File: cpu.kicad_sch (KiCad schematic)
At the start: 37 parts, among them J11 Debug, J12 GPS_Snoop, J13 I2C_Snoop, J7 USB_C_Receptacle_16P, U4 STM32H503KBUx, Y1 32768Hz

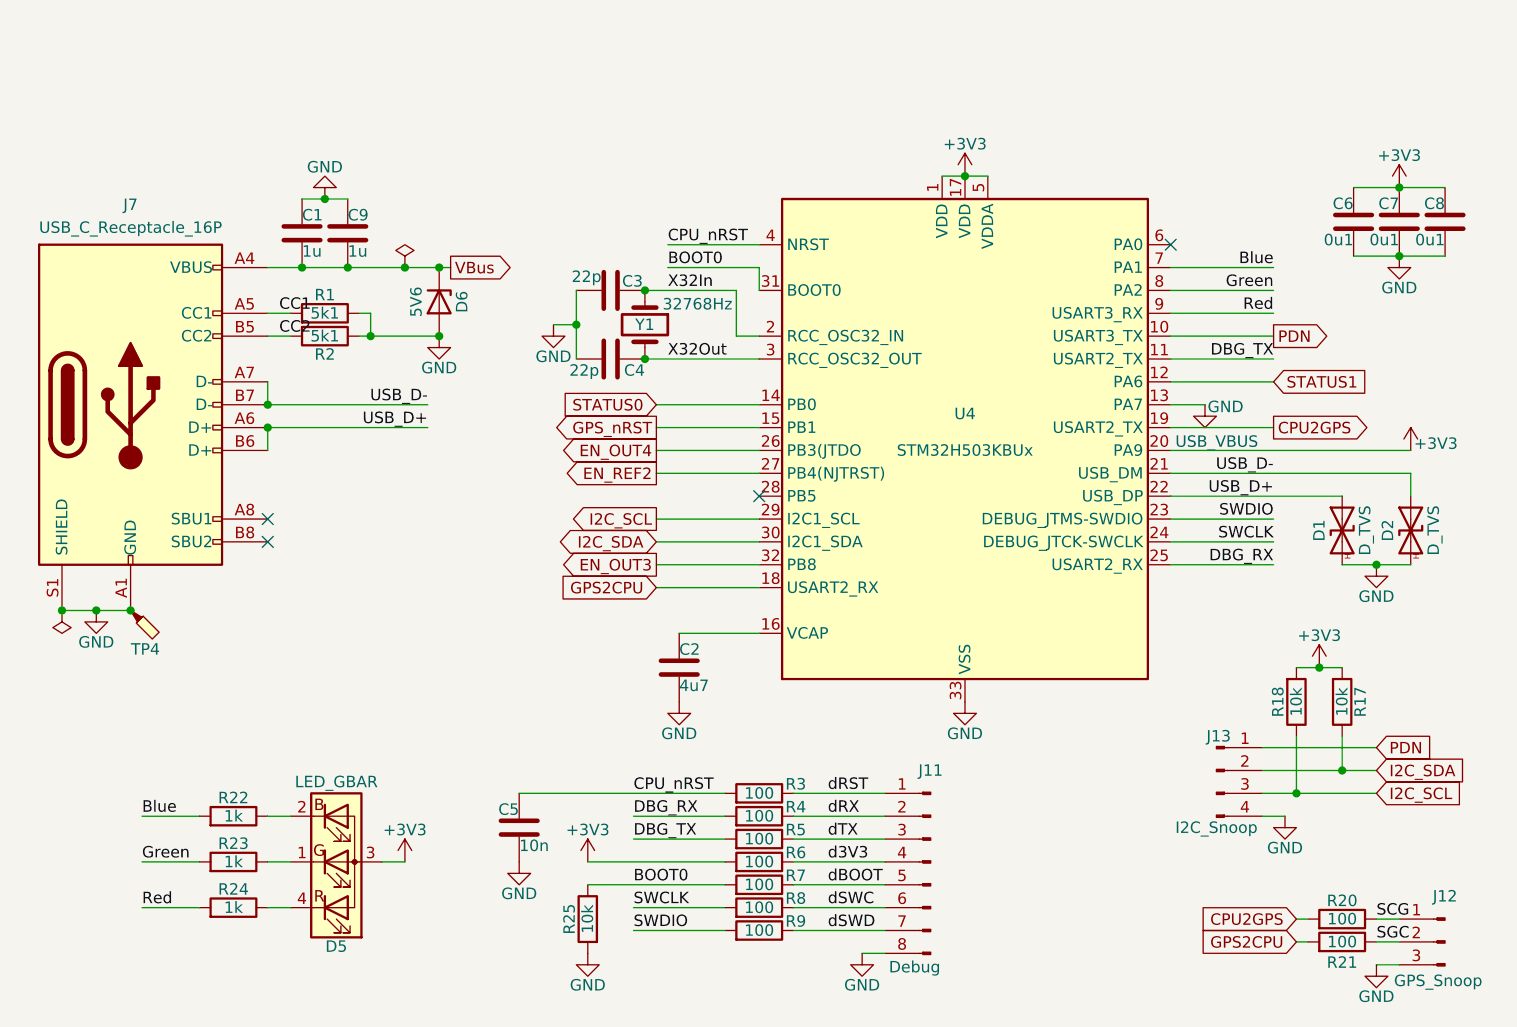
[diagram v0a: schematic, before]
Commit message: Squeeze in a connector to break out GPS.
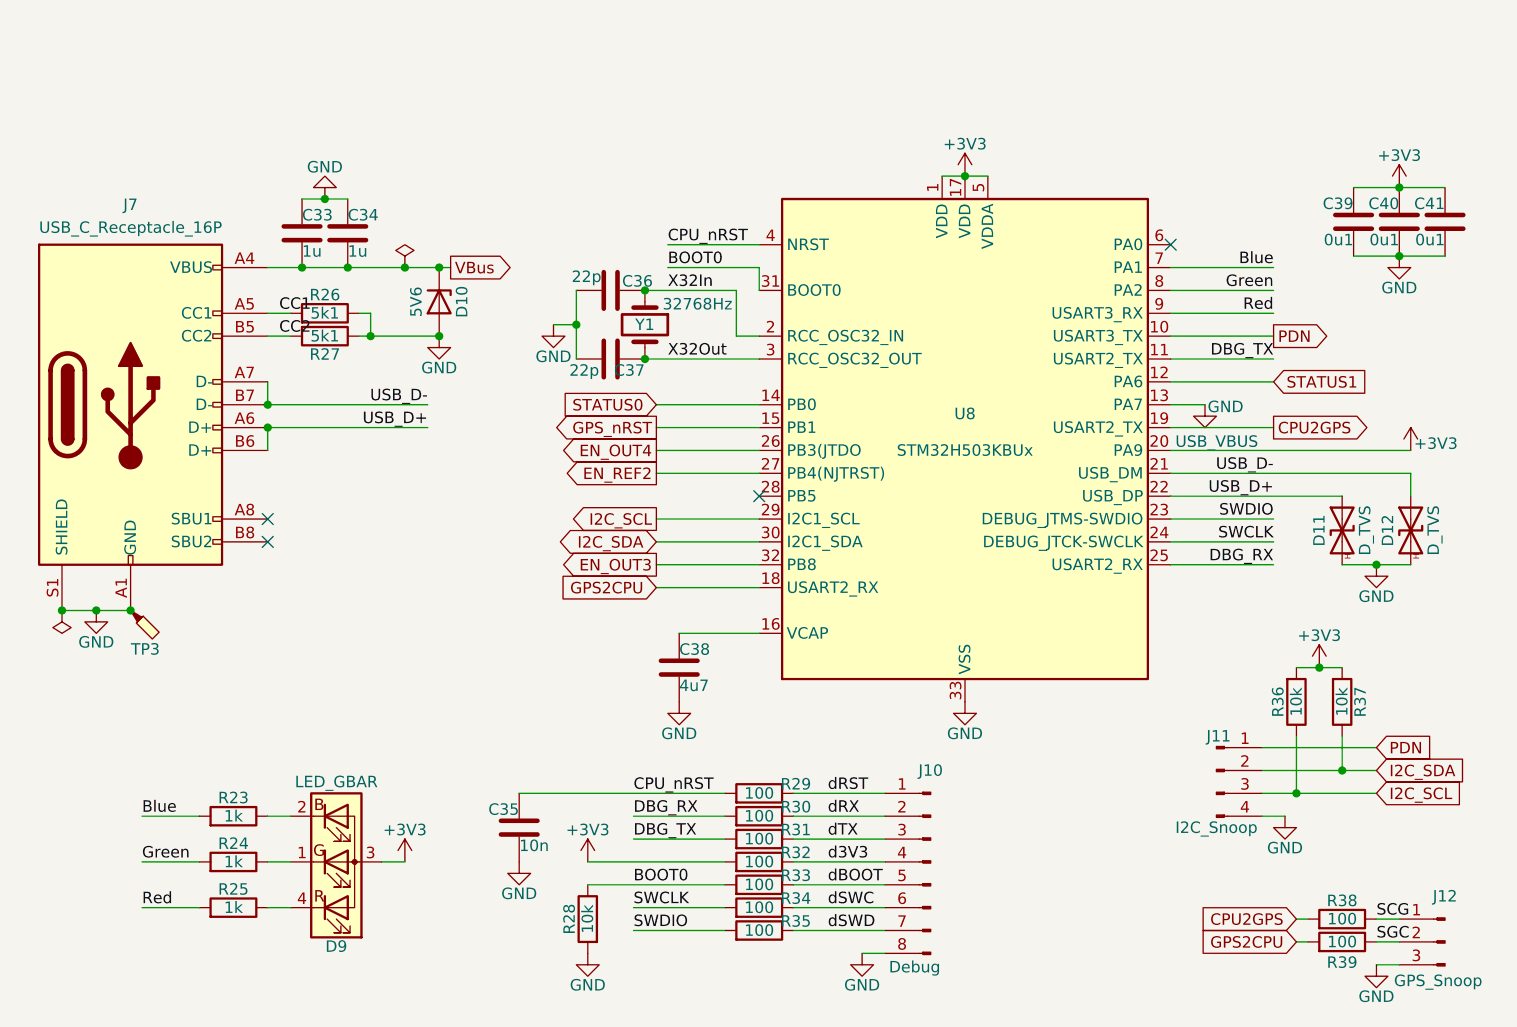
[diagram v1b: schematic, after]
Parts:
- renumbered C1 to C33, C9 to C34, C5 to C35, C3 to C36, C4 to C37, C2 to C38, C6 to C39, C7 to C40, C8 to C41, D6 to D10, D1 to D11, D2 to D12, D5 to D9, J11 to J10, J13 to J11, R22 to R23, R23 to R24, R24 to R25, R1 to R26, R2 to R27, R25 to R28, R3 to R29, R4 to R30, R5 to R31, R6 to R32, R7 to R33, R8 to R34, R9 to R35, R18 to R36, R17 to R37, R20 to R38, R21 to R39, TP4 to TP3, U4 to U8

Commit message: Silkscreen passes DRC.  Also we renumbered everything.
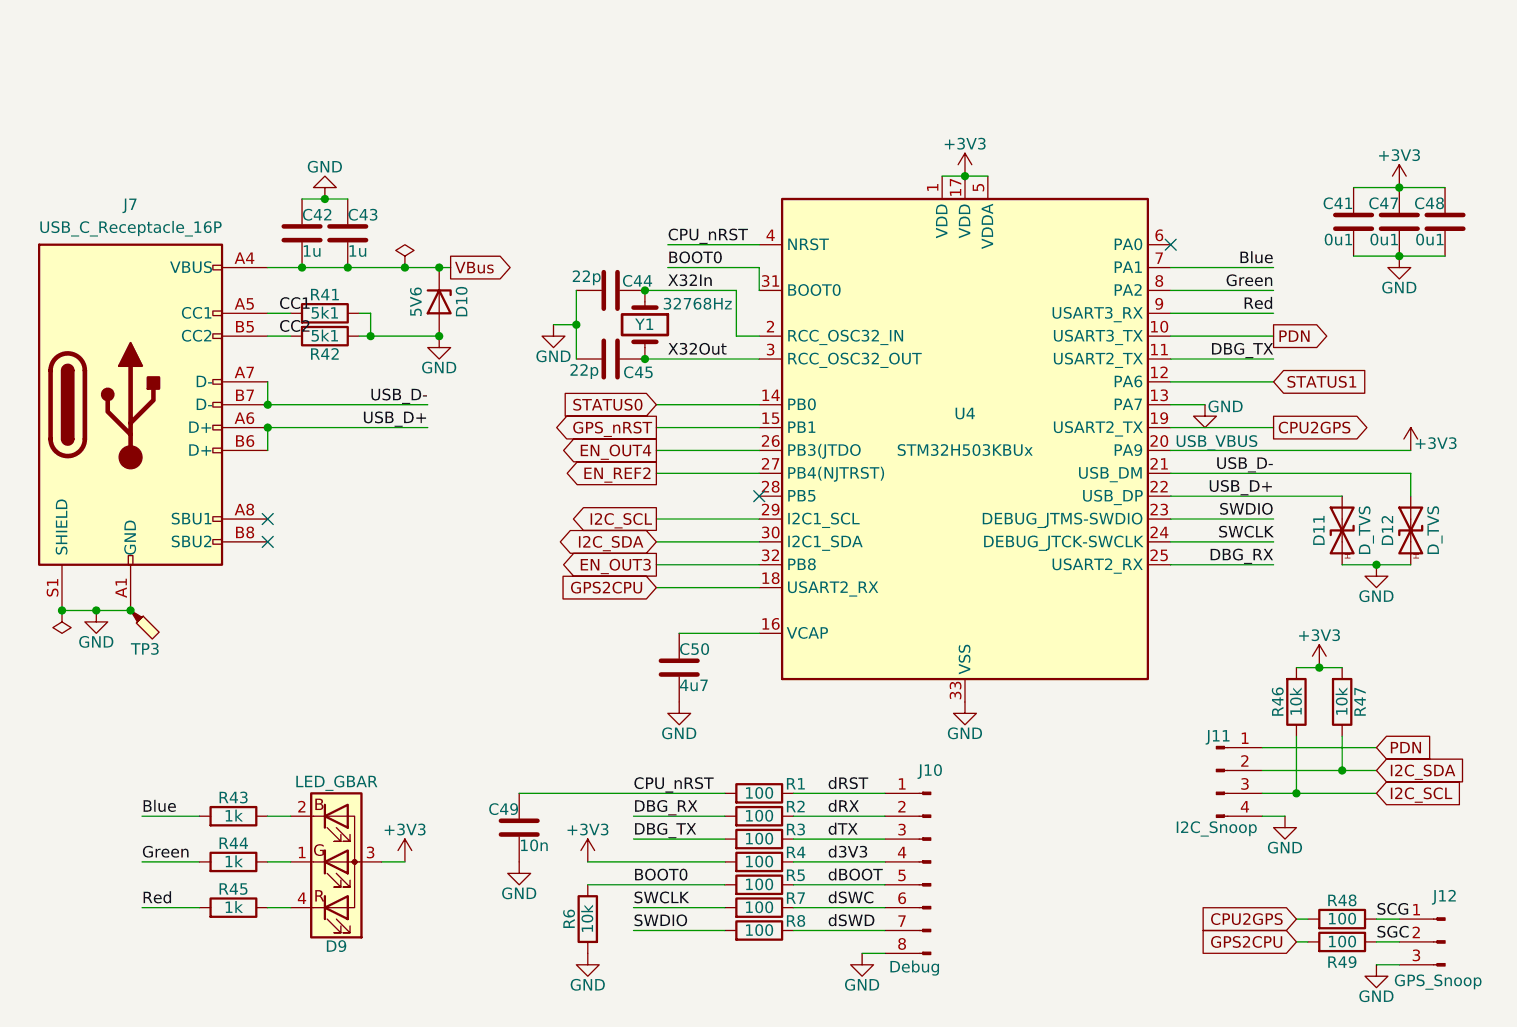
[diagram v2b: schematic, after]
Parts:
- renumbered C39 to C41, C33 to C42, C34 to C43, C36 to C44, C37 to C45, C40 to C47, C41 to C48, C35 to C49, C38 to C50, R29 to R1, R30 to R2, R31 to R3, R32 to R4, R26 to R41, R27 to R42, R23 to R43, R24 to R44, R25 to R45, R36 to R46, R37 to R47, R38 to R48, R39 to R49, R33 to R5, R28 to R6, R34 to R7, R35 to R8, U8 to U4

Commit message: Sorting out part number assignments.
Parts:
- C41, C47, C48: JLCPCB C307331 -> (none); LCSC (none) -> C307331
- C42, C43: JLCPCB C52923 -> (none); LCSC (none) -> C52923
- C44, C45: JLCPCB C1555 -> (none); LCSC (none) -> C1555
- C49: JLCPCB C15195 -> (none); LCSC (none) -> C15195
- C50: JLCPCB C23733 -> (none); LCSC (none) -> C23733
- D10: JLCPCB C19077435 -> (none); LCSC (none) -> C19077435
- R1, R2, R3, R4, R48, R49, R5, R7, R8: JLCPCB C25076 -> (none); LCSC (none) -> C25076
- R41, R42: JLCPCB C25905 -> (none); LCSC (none) -> C25905
- R43, R44, R45: JLCPCB C11702 -> (none); LCSC (none) -> C11702
- R46, R47, R6: JLCPCB C25744 -> (none); LCSC (none) -> C25744
- U4: JLCPCB C22385521 -> (none); LCSC (none) -> C22385521
- Y1: JLCPCB C32346 -> (none); LCSC (none) -> C32346

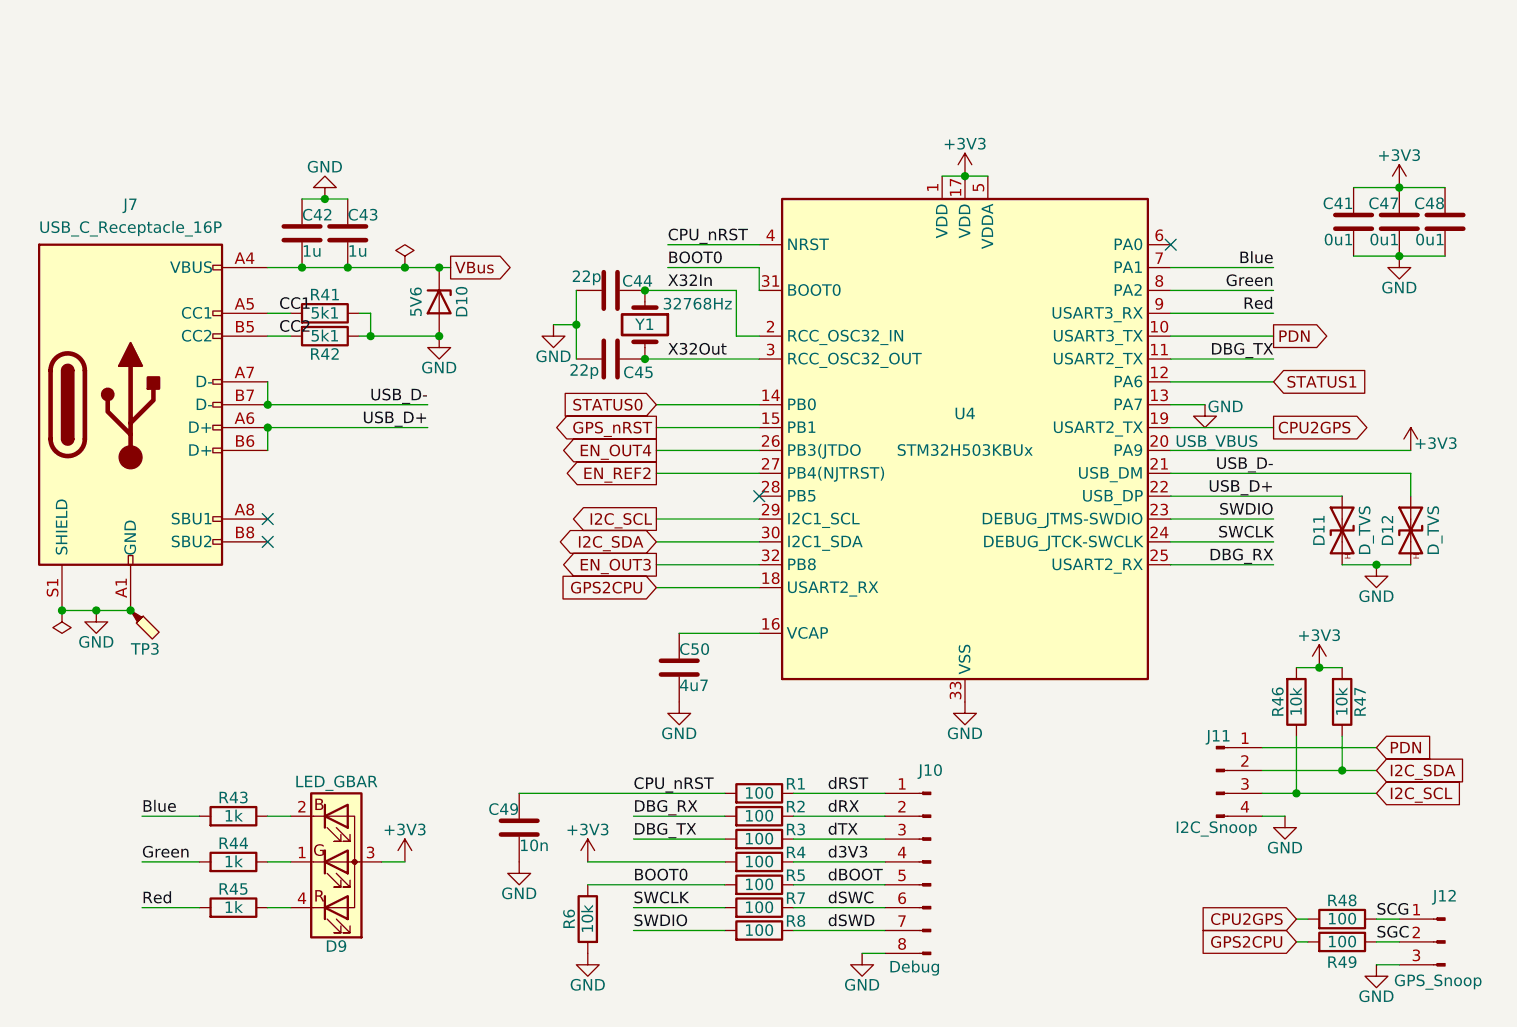
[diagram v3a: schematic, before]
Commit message: Change the programming connector.
Change the SMA footprint to match narrow ones.
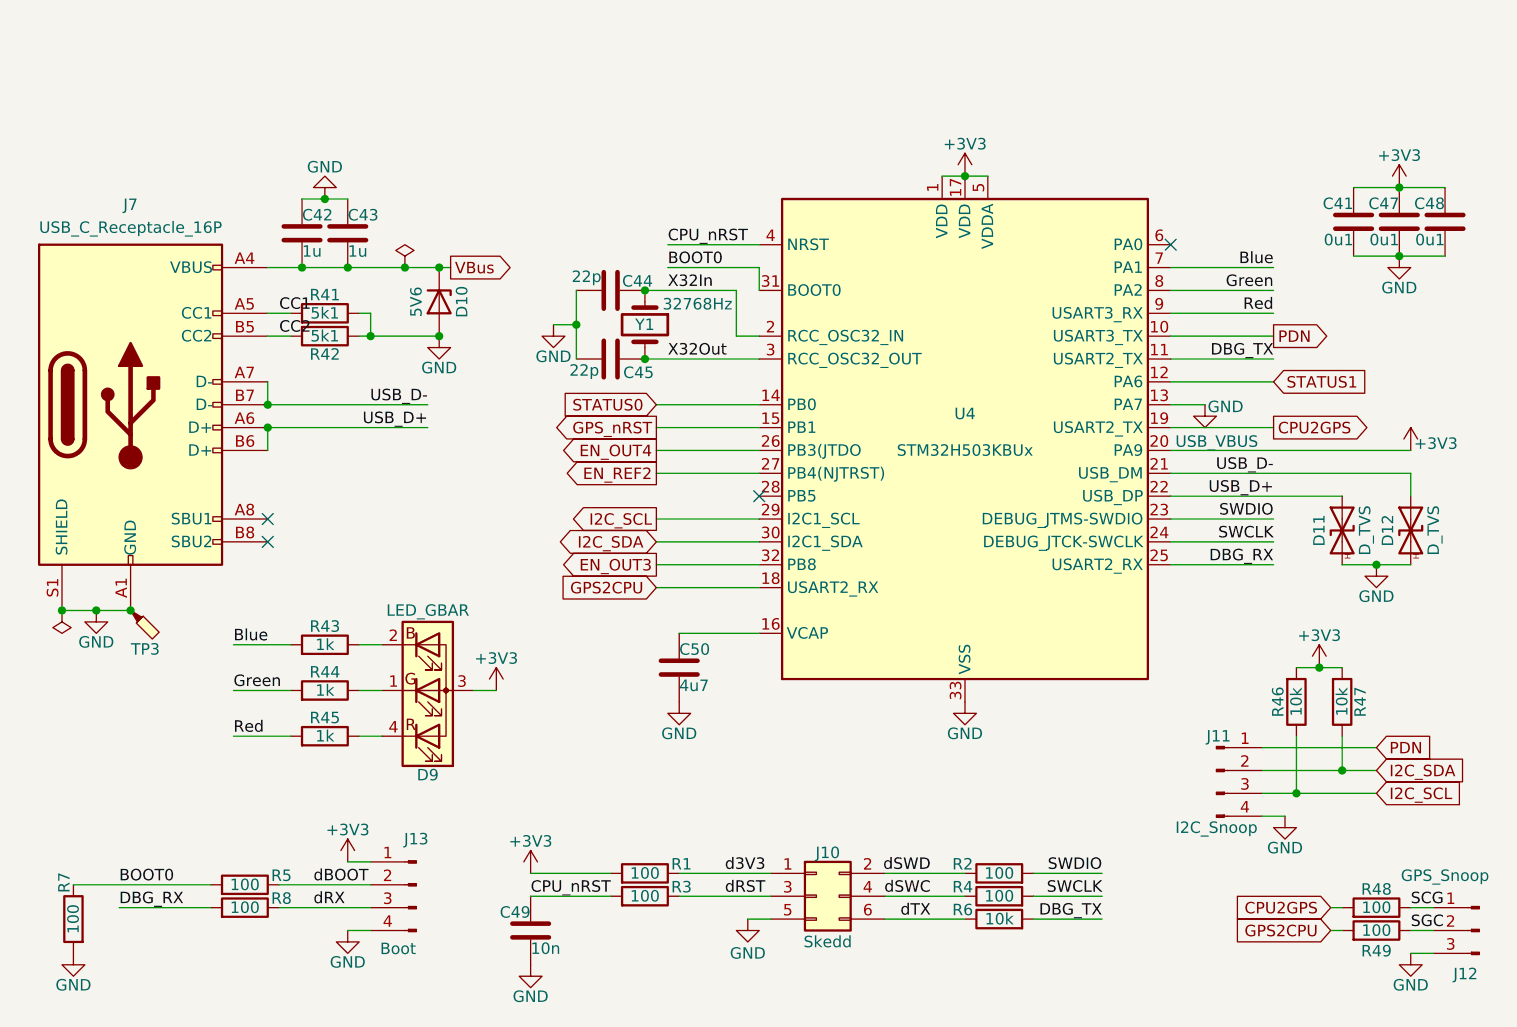
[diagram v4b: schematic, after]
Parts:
- removed J10: Debug, Parts:PinHeader_1x08_P2.54mm_Vertical, symbol Connector:Conn_01x08_Pin
- added J10: Skedd, Parts:Skedd6, symbol Connector_Generic:Conn_02x03_Odd_Even
- added J13: Boot, Parts:PinHeader_1x04_P2.54mm_Vertical, symbol Connector:Conn_01x04_Pin
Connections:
- net +3V3: now also R1.2, J13.1 (Pin_1); no longer R4.2
- net BOOT0: now also R7.1; no longer R6.1
- net CPU_nRST: now also R3.2; no longer R1.2
- net DBG_RX: now also R8.2; no longer R2.2
- net DBG_TX: now also R6.2; no longer R3.2
- net GND: now also R7.2, J10.5 (Pin_5), J13.4 (Pin_4); no longer R6.2
- net SWCLK: now also R4.2; no longer R7.2
- net SWDIO: now also R2.2; no longer R8.2
- net d3V3: now also R1.1, J10.1 (Pin_1); no longer R4.1
- net dBOOT: now also J13.2 (Pin_2)
- net dRST: now also R3.1, J10.3 (Pin_3); no longer R1.1
- net dRX: now also R8.1, J13.3 (Pin_3); no longer R2.1
- net dSWC: now also R4.1, J10.4 (Pin_4); no longer R7.1
- net dSWD: now also R2.1, J10.2 (Pin_2); no longer R8.1
- net dTX: now also R6.1, J10.6 (Pin_6); no longer R3.1
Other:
- moved on the sheet: C49, D9, J12, R1, R2, R3, R4, R43, R44, R45, R48, R49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

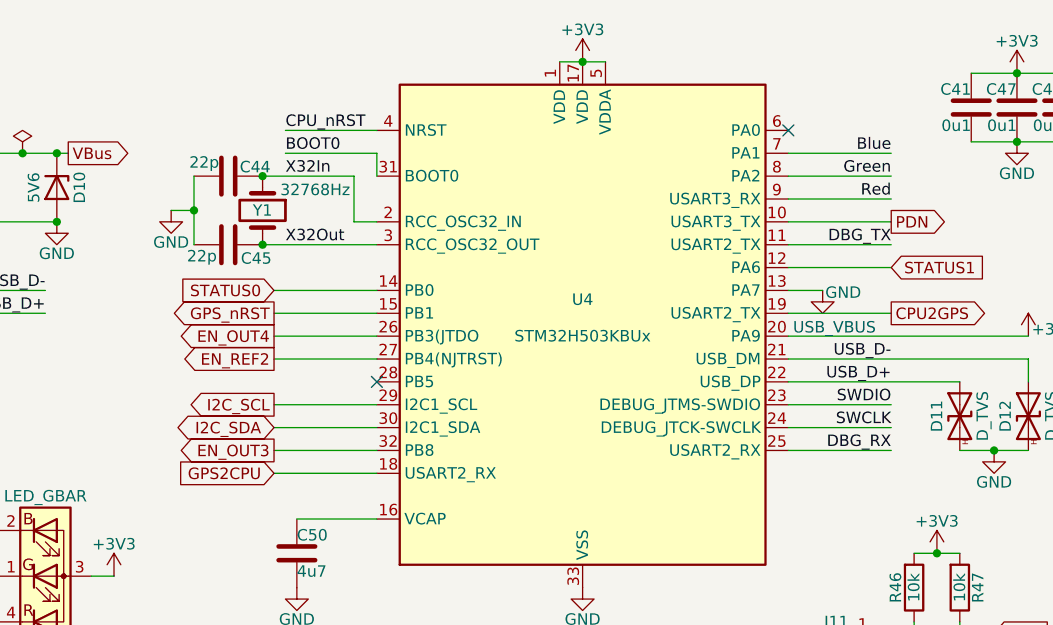
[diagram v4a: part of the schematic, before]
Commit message: Tidy up pinout.
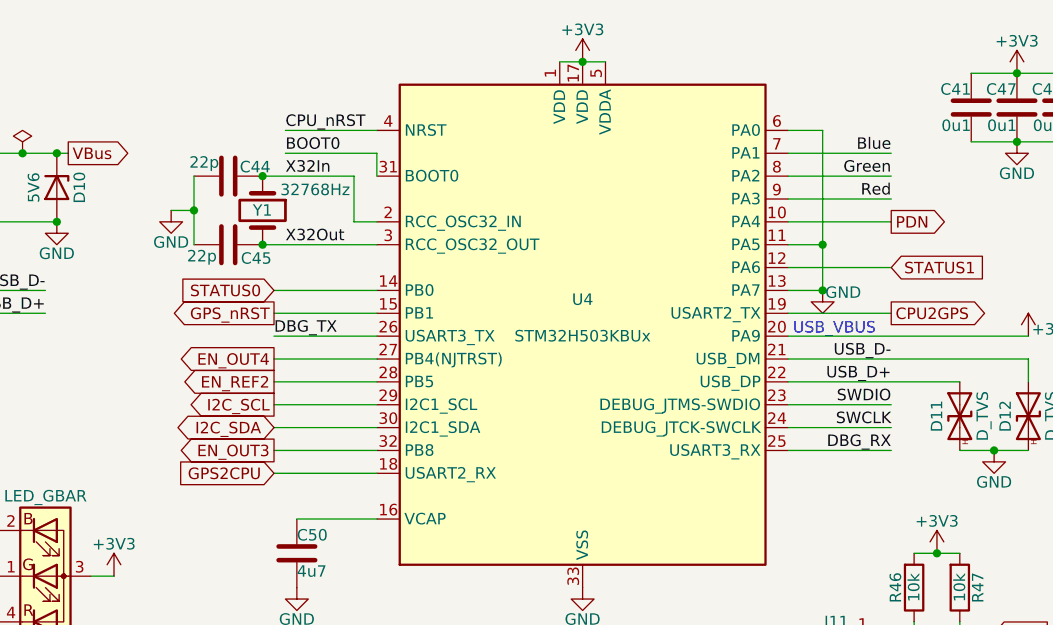
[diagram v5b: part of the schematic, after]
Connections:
- net DBG_TX: now also U4.26 (PB3(JTDO); no longer U4.11 (PA5)
- net EN_OUT4: now also U4.27 (PB4(NJTRST)); no longer U4.26 (PB3(JTDO)
- net EN_REF2: now also U4.28 (PB5); no longer U4.27 (PB4(NJTRST))
- net GND: now also U4.11 (PA5), U4.6 (PA0)
- no-connect marks 4 -> 2

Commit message: Ready for respin.
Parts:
- J10, J13: now left out of the parts list
